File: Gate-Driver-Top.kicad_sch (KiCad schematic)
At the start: 12 parts, among them J1 Conn_01x02, U1 ISO5452QDWQ1

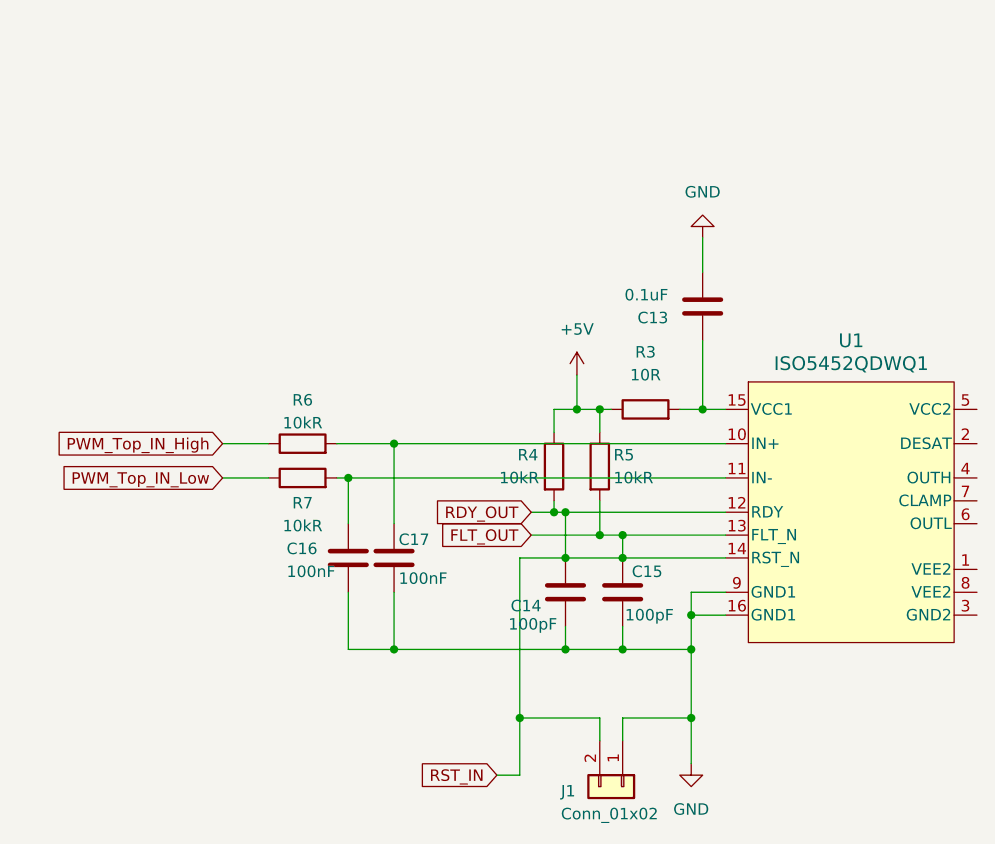
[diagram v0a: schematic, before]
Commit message: gate driver added
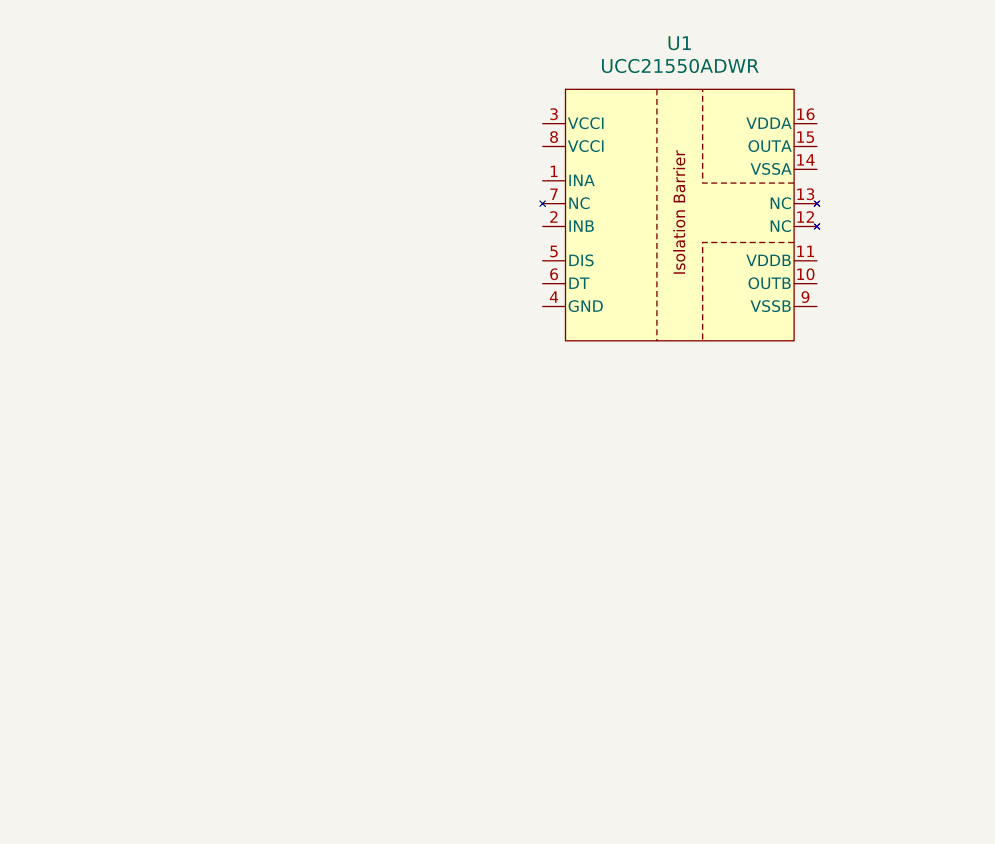
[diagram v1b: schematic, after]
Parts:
- removed C13: 0.1uF, Capacitor_SMD:C_0805_2012Metric, symbol Device:C
- removed C14, C15: 100pF, Capacitor_SMD:C_0805_2012Metric, symbol Device:C
- removed C16, C17: 100nF, Capacitor_SMD:C_0805_2012Metric, symbol Device:C
- removed J1: Conn_01x02, Connector_PinHeader_2.54mm:PinHeader_1x02_P2.54mm_Vertical, symbol Connector_Generic:Conn_01x02
- removed R3: 10R, Resistor_SMD:R_0805_2012Metric, symbol Device:R
- removed R4, R5, R6, R7: 10kR, Resistor_SMD:R_0805_2012Metric, symbol Device:R
- removed U1: ISO5452QDWQ1, gate_drivers:DW0016B_HV, symbol Library-N1-Gate-Driver:ISO5452QDWQ1
- added U1: UCC21550ADWR, gate_drivers:SOIC16_DW_TEX-L, symbol Library-N1-Gate-Driver:UCC21550ADWR

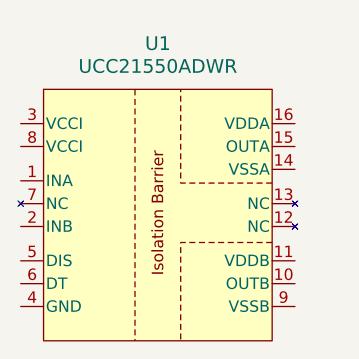
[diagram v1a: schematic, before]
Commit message: added LM1117-5.0
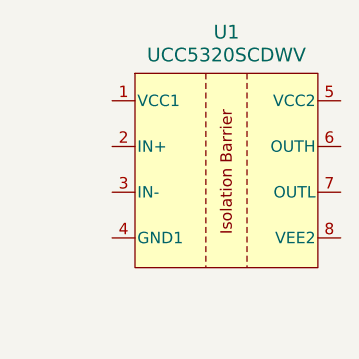
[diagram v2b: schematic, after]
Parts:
- removed U1: UCC21550ADWR, gate_drivers:SOIC16_DW_TEX-L, symbol Library-N1-Gate-Driver:UCC21550ADWR
- added U1: UCC5320SCDWV, gate_drivers:DWV0008A-IPC_B, symbol Library-N1-Gate-Driver:UCC5320SCDWV
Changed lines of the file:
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@@
 	(paper "A4")
 	(symbol
-		(lib_id "Library-N1-Gate-Driver:UCC21550ADWR")
-		(at 132.08 64.77 0)
+		(lib_id "Library-N1-Gate-Driver:UCC5320SCDWV")
+		(at 139.7 60.96 0)
 		(unit 1)
 		(exclude_from_sim no)
@@
 		(fields_autoplaced yes)
 		(property "Reference" "U1"
-			(at 132.08 46.99 0)
+			(at 139.7 45.72 0)
 			(effects
 				(font
@@
 			)
 		)
-		(property "Value" "UCC21550ADWR"
-			(at 132.08 49.53 0)
+		(property "Value" "UCC5320SCDWV"
+			(at 139.7 48.26 0)
 			(effects
 				(font
@@
 			)
 		)
-		(property "Footprint" "gate_drivers:SOIC16_DW_TEX-L"
-			(at 130.81 40.132 0)
+		(property "Footprint" "gate_drivers:DWV0008A-IPC_B"
+			(at 140.97 60.706 0)
 			(effects
 				(font
@@
 			)
 		)
-		(property "Datasheet" "https://www.ti.com/lit/gpn/ucc21550"
-			(at 133.858 37.592 0)
+		(property "Datasheet" "https://www.ti.com/lit/gpn/ucc5320"
+			(at 140.97 60.706 0)
 			(effects
 				(font
@@
 		)
 		(property "Description" ""
-			(at 132.08 64.77 0)
+			(at 139.7 60.96 0)
 			(effects
 				(font
@@
 			)
 		)
-		(pin "14"
+		(pin "8"
 		)
-		(pin "12"
+		(pin "2"
 		)
-		(pin "10"
-		)
-		(pin "9"
-		)
-		(pin "13"
-		)
-		(pin "11"
-		)
-		(pin "7"
+		(pin "4"
 		)
 		(pin "5"
@@
 		(pin "1"
 		)
-		(pin "2"
-		)
-		(pin "16"
-		)
-		(pin "15"
+		(pin "7"
 		)
 		(pin "3"
 		)
-		(pin "8"
-		)
 		(pin "6"
 		)
-		(pin "4"
-		)
 		(instances
